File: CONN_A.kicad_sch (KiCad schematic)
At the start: 1 part, among them J4 6437288-4

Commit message: lsd circuit in place
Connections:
- net +12V renamed 12V
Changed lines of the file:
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@@
 			)
 		)
-		(property "Value" "+12V"
+		(property "Value" "12V"
 			(at 27.686 20.066 0)
 			(effects
@@
 			)
 		)
-		(property "Value" "+12V"
+		(property "Value" "12V"
 			(at 54.356 58.674 0)
 			(effects

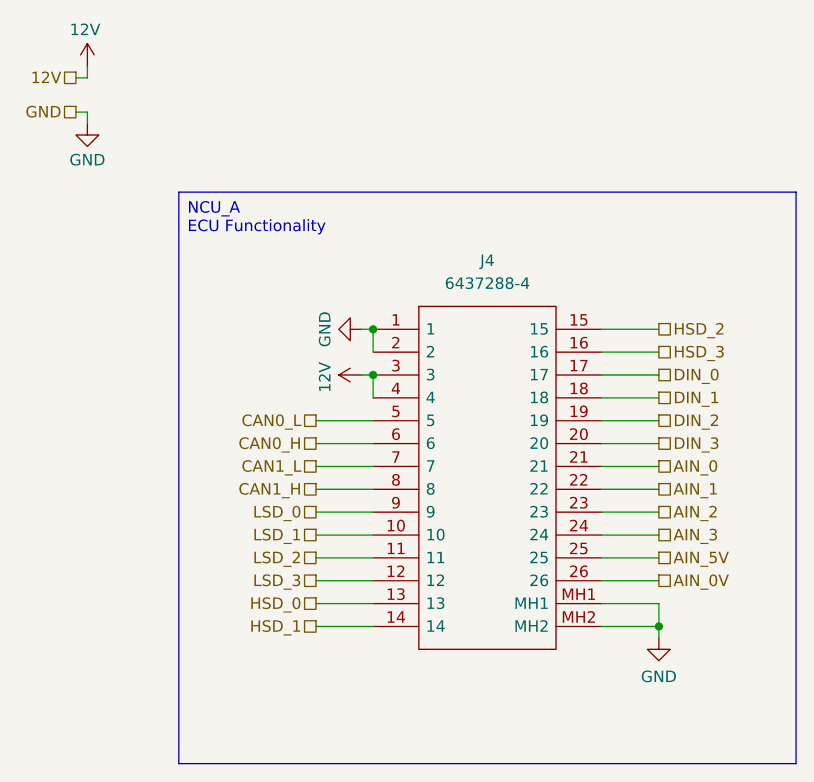
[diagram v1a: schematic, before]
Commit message: added 3.3v gpio input protection
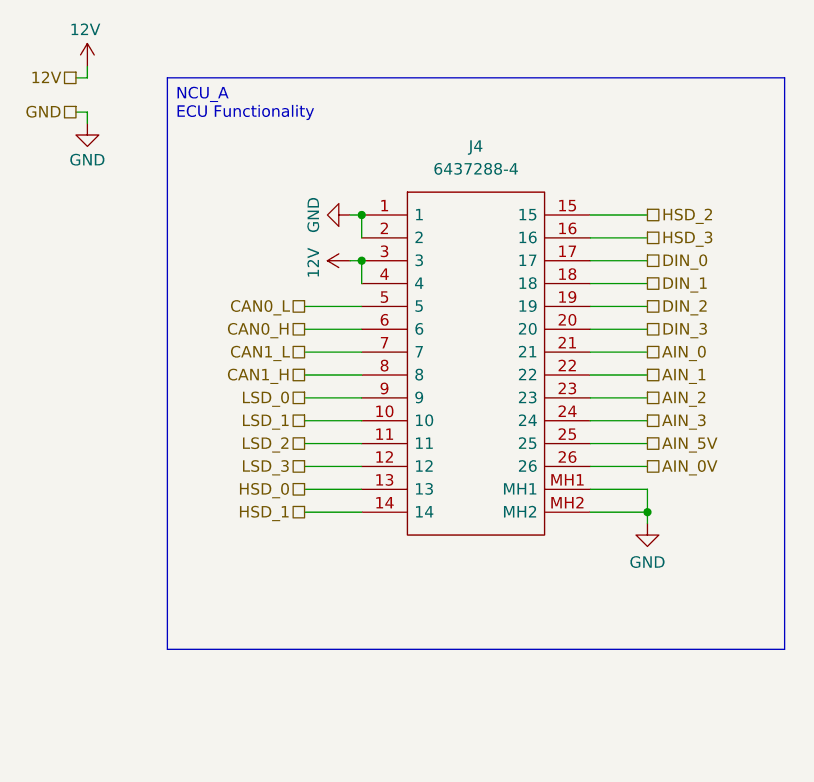
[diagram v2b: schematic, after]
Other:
- moved on the sheet: J4

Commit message: redid annotations, added test point
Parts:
- renumbered J4 to J1
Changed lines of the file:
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@@
 		(on_board yes)
 		(dnp no)
-		(property "Reference" "#PWR093"
+		(property "Reference" "#PWR038"
 			(at 27.94 27.94 0)
 			(effects
@@
 			(project "NCU"
 				(path "/3aee14c3-5480-4f7c-989e-3fef81779034/76e9985e-671f-4dd1-8bb7-de1ef0777d71"
-					(reference "#PWR093")
+					(reference "#PWR038")
 					(unit 1)
 				)
@@
 		(on_board yes)
 		(dnp no)
-		(property "Reference" "#PWR084"
+		(property "Reference" "#PWR042"
 			(at 90.17 81.28 0)
 			(effects
@@
 			(project "NCU"
 				(path "/3aee14c3-5480-4f7c-989e-3fef81779034/76e9985e-671f-4dd1-8bb7-de1ef0777d71"
-					(reference "#PWR084")
+					(reference "#PWR042")
 					(unit 1)
 				)
@@
 		(on_board yes)
 		(dnp no)
-		(property "Reference" "#PWR085"
+		(property "Reference" "#PWR040"
 			(at 50.8 40.64 0)
 			(effects
@@
 			(project "NCU"
 				(path "/3aee14c3-5480-4f7c-989e-3fef81779034/76e9985e-671f-4dd1-8bb7-de1ef0777d71"
-					(reference "#PWR085")
+					(reference "#PWR040")
 					(unit 1)
 				)
@@
 		(dnp no)
 		(fields_autoplaced yes)
-		(property "Reference" "J4"
+		(property "Reference" "J1"
 			(at 71.12 33.02 0)
 			(effects
@@
 			(project "NCU"
 				(path "/3aee14c3-5480-4f7c-989e-3fef81779034/76e9985e-671f-4dd1-8bb7-de1ef0777d71"
-					(reference "J4")
+					(reference "J1")
 					(unit 1)
 				)
@@
 		(on_board yes)
 		(dnp no)
-		(property "Reference" "#PWR0106"
+		(property "Reference" "#PWR041"
 			(at 60.96 45.72 0)
 			(effects
@@
 			(project "NCU"
 				(path "/3aee14c3-5480-4f7c-989e-3fef81779034/76e9985e-671f-4dd1-8bb7-de1ef0777d71"
-					(reference "#PWR0106")
+					(reference "#PWR041")
 					(unit 1)
 				)
@@
 		(on_board yes)
 		(dnp no)
-		(property "Reference" "#PWR092"
+		(property "Reference" "#PWR039"
 			(at 27.94 36.83 0)
 			(effects
@@
 			(project "NCU"
 				(path "/3aee14c3-5480-4f7c-989e-3fef81779034/76e9985e-671f-4dd1-8bb7-de1ef0777d71"
-					(reference "#PWR092")
-					(unit 1)
-				)
+					(reference "#PWR039")
+					(unit 1)
+				)
